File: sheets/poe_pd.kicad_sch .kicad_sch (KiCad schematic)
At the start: 30 parts, among them J1 0826-1X1T-HS-F, U1 DFLS130LQ-7, U2 DFLS130LQ-7, U3 DFLS130LQ-7, U4 DFLS130LQ-7, U5 TPS2372-4RGWR

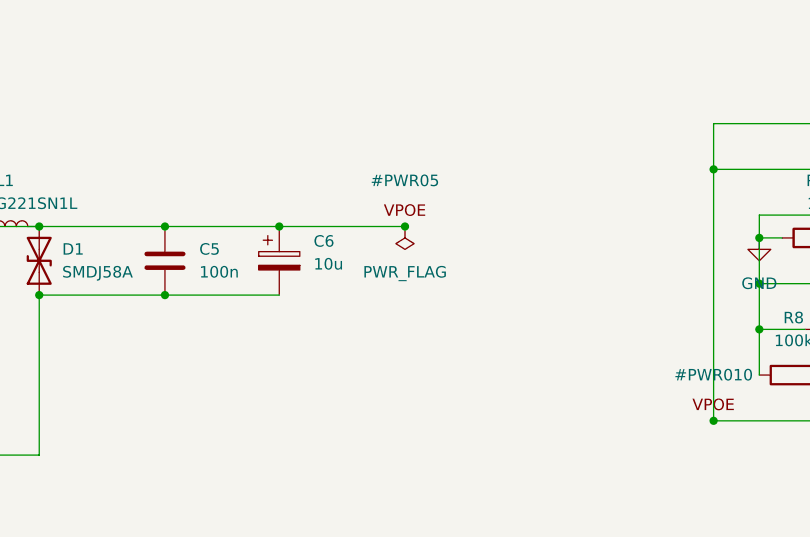
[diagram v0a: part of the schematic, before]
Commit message: Complete Sheet 4 - Amp Stage TAS3251
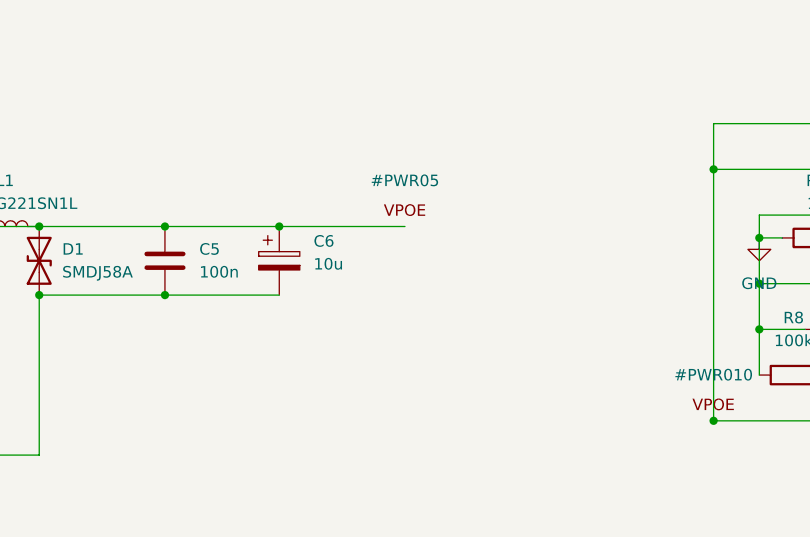
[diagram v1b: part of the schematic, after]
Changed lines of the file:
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@@
 	(paper "A4")
 	(junction
-		(at 153.67 55.88)
-		(diameter 0)
-		(color 0 0 0 0)
-	)
-	(junction
 		(at 139.7 55.88)
 		(diameter 0)
@@
 					(unit 1)
 				)
-			)
-		)
-	)
-	(symbol
-		(lib_id "power:PWR_FLAG")
-		(at 153.67 55.88 180)
-		(unit 1)
-		(body_style 1)
-		(exclude_from_sim no)
-		(in_bom yes)
-		(on_board yes)
-		(in_pos_files yes)
-		(dnp no)
-		(fields_autoplaced yes)
-		(property "Reference" "#FLG01"
-			(at 153.67 57.785 0)
-			(hide yes)
-			(show_name no)
-			(do_not_autoplace no)
-			(effects
-				(font
-					(size 1.27 1.27)
-				)
-			)
-		)
-		(property "Value" "PWR_FLAG"
-			(at 153.67 60.96 0)
-			(show_name no)
-			(do_not_autoplace no)
-			(effects
-				(font
-					(size 1.27 1.27)
-				)
-			)
-		)
-		(property "Footprint" ""
-			(at 153.67 55.88 0)
-			(hide yes)
-			(show_name no)
-			(do_not_autoplace no)
-			(effects
-				(font
-					(size 1.27 1.27)
-				)
-			)
-		)
-		(property "Datasheet" ""
-			(at 153.67 55.88 0)
-			(hide yes)
-			(show_name no)
-			(do_not_autoplace no)
-			(effects
-				(font
-					(size 1.27 1.27)
-				)
-			)
-		)
-		(property "Description" "Special symbol for telling ERC where power comes from"
-			(at 153.67 55.88 0)
-			(hide yes)
-			(show_name no)
-			(do_not_autoplace no)
-			(effects
-				(font
-					(size 1.27 1.27)
-				)
-			)
-		)
-		(pin "1"
-		)
-		(instances
-			(project "poe-aes67-amp"
-				(path "/342711d1-e6c4-426d-85fd-6094774cf2a5/693c70d2-0654-43ac-9c2d-6cfb6d40fe72"
-					(reference "#FLG01")
-					(unit 1)
-				)

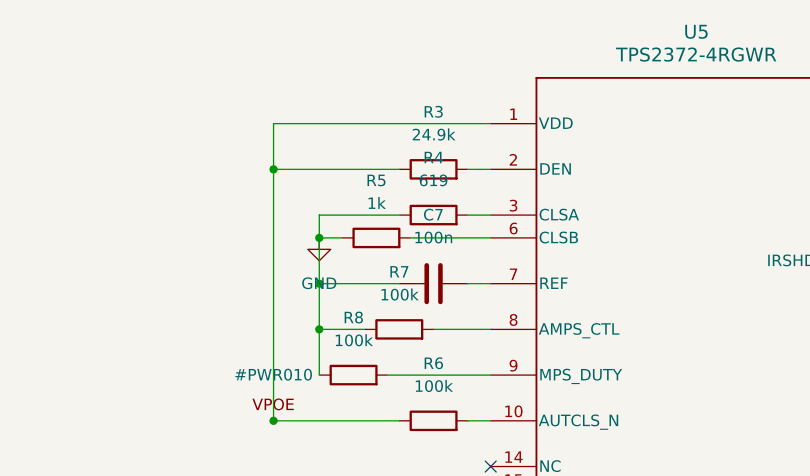
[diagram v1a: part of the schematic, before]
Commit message: Complete datasheet audit and fixes across Sheets 2, 3 and 4
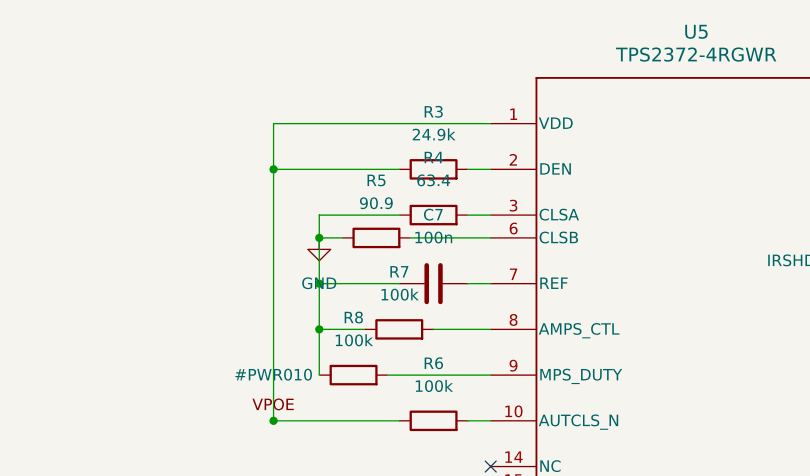
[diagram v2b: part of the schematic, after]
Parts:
- R4: value 619 -> 63.4
- R5: value 1k -> 90.9
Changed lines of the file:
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@@
 			)
 		)
-		(property "Value" "1k"
+		(property "Value" "90.9"
 			(at 199.39 53.34 90)
 			(show_name no)
@@
 			)
 		)
-		(property "Value" "619"
+		(property "Value" "63.4"
 			(at 205.74 50.8 90)
 			(show_name no)
